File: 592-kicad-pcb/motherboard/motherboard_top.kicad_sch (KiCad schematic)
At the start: 31 parts, among them J21 Conn_02x01, J22 Conn_02x01, J23 Conn_02x01, J24 Conn_02x01, J25 Conn_02x01, J26 Conn_02x01, U15 SN74LVC1G14DBV, U16 SN74LVC1G00DCK, U17 74CBTLV3257PW,118, U18 SN74LVC1G14DBV, U19 74CBTLV3257PW,118, U20 74CBTLV3257PW,118, U21 74CBTLV3257PW,118

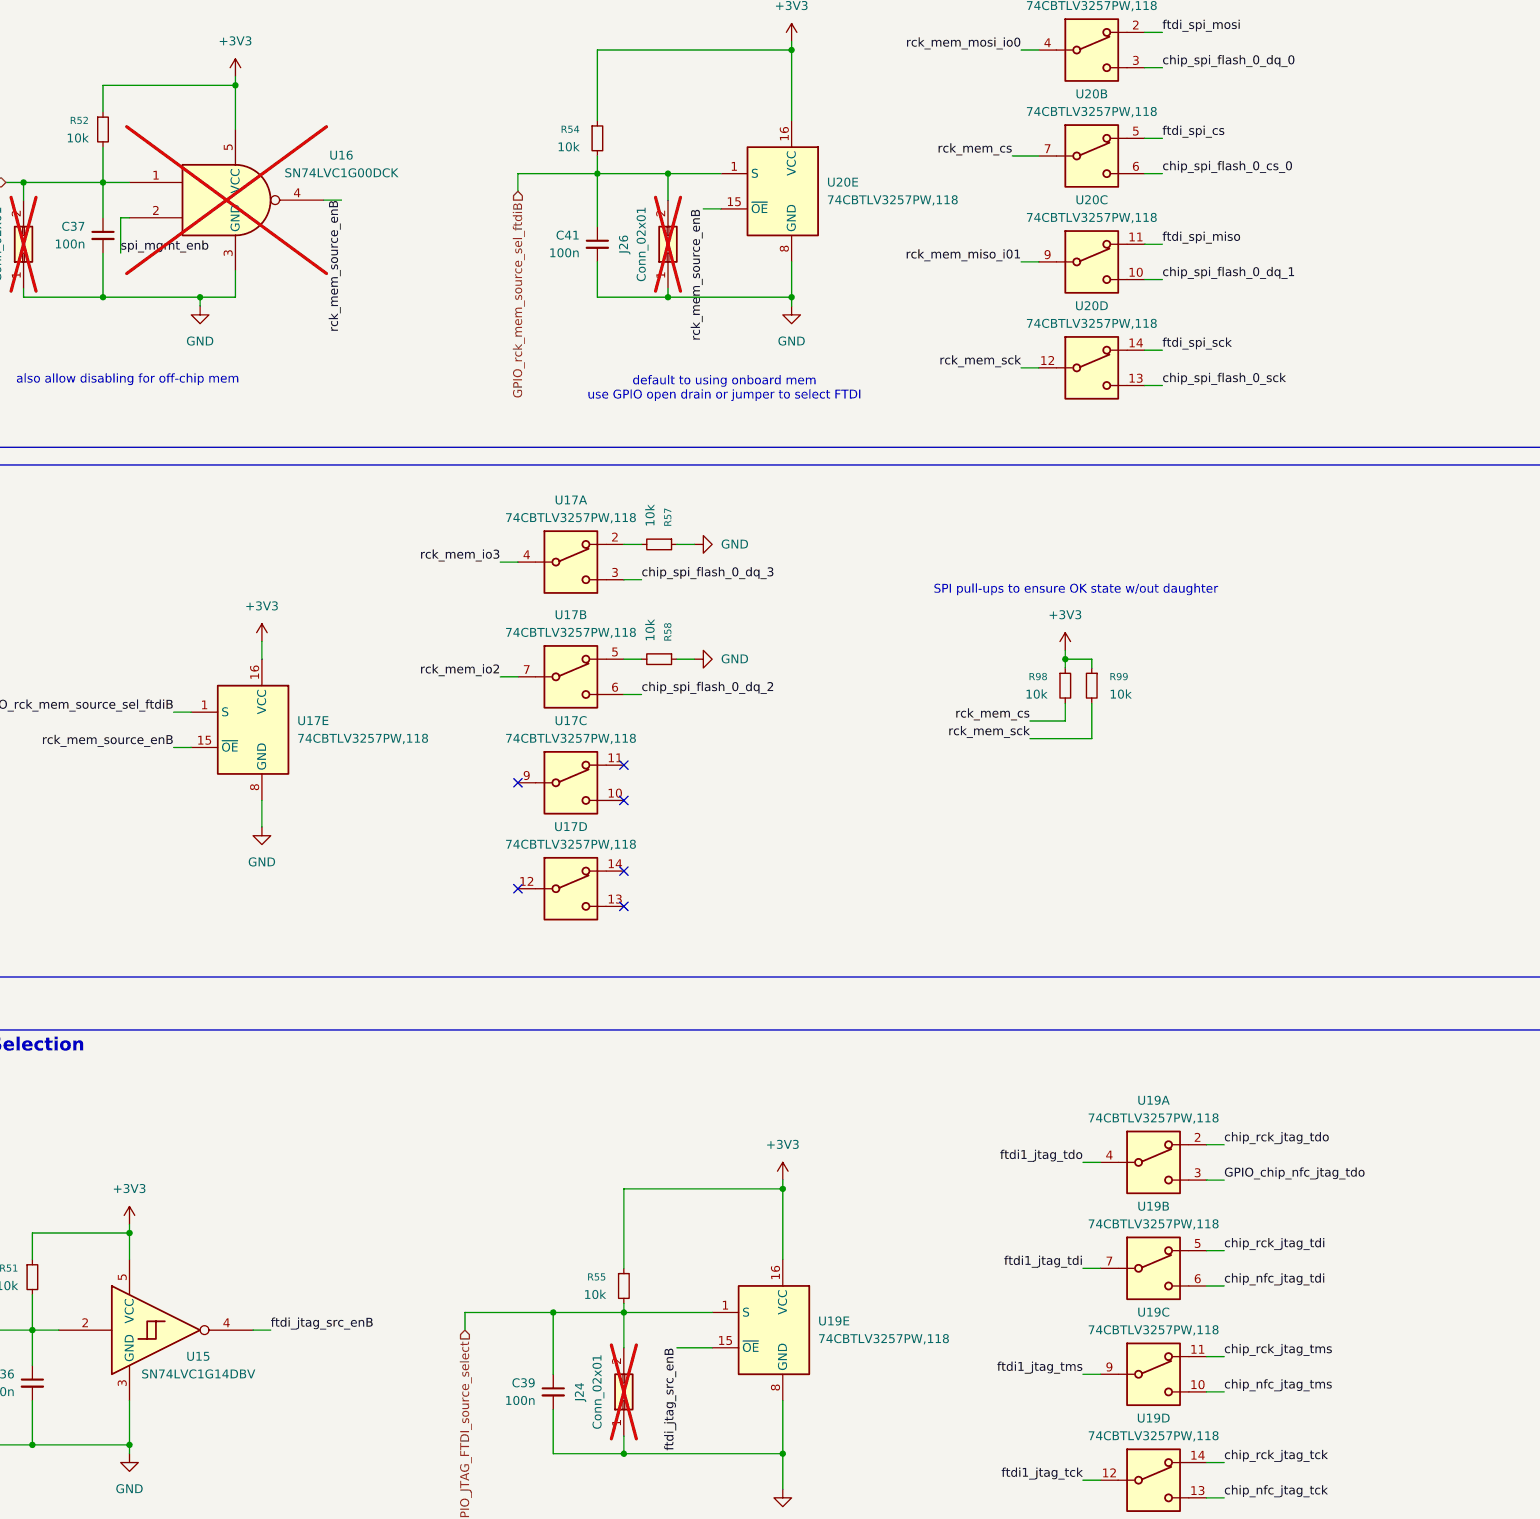
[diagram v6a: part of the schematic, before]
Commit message: core routing progress
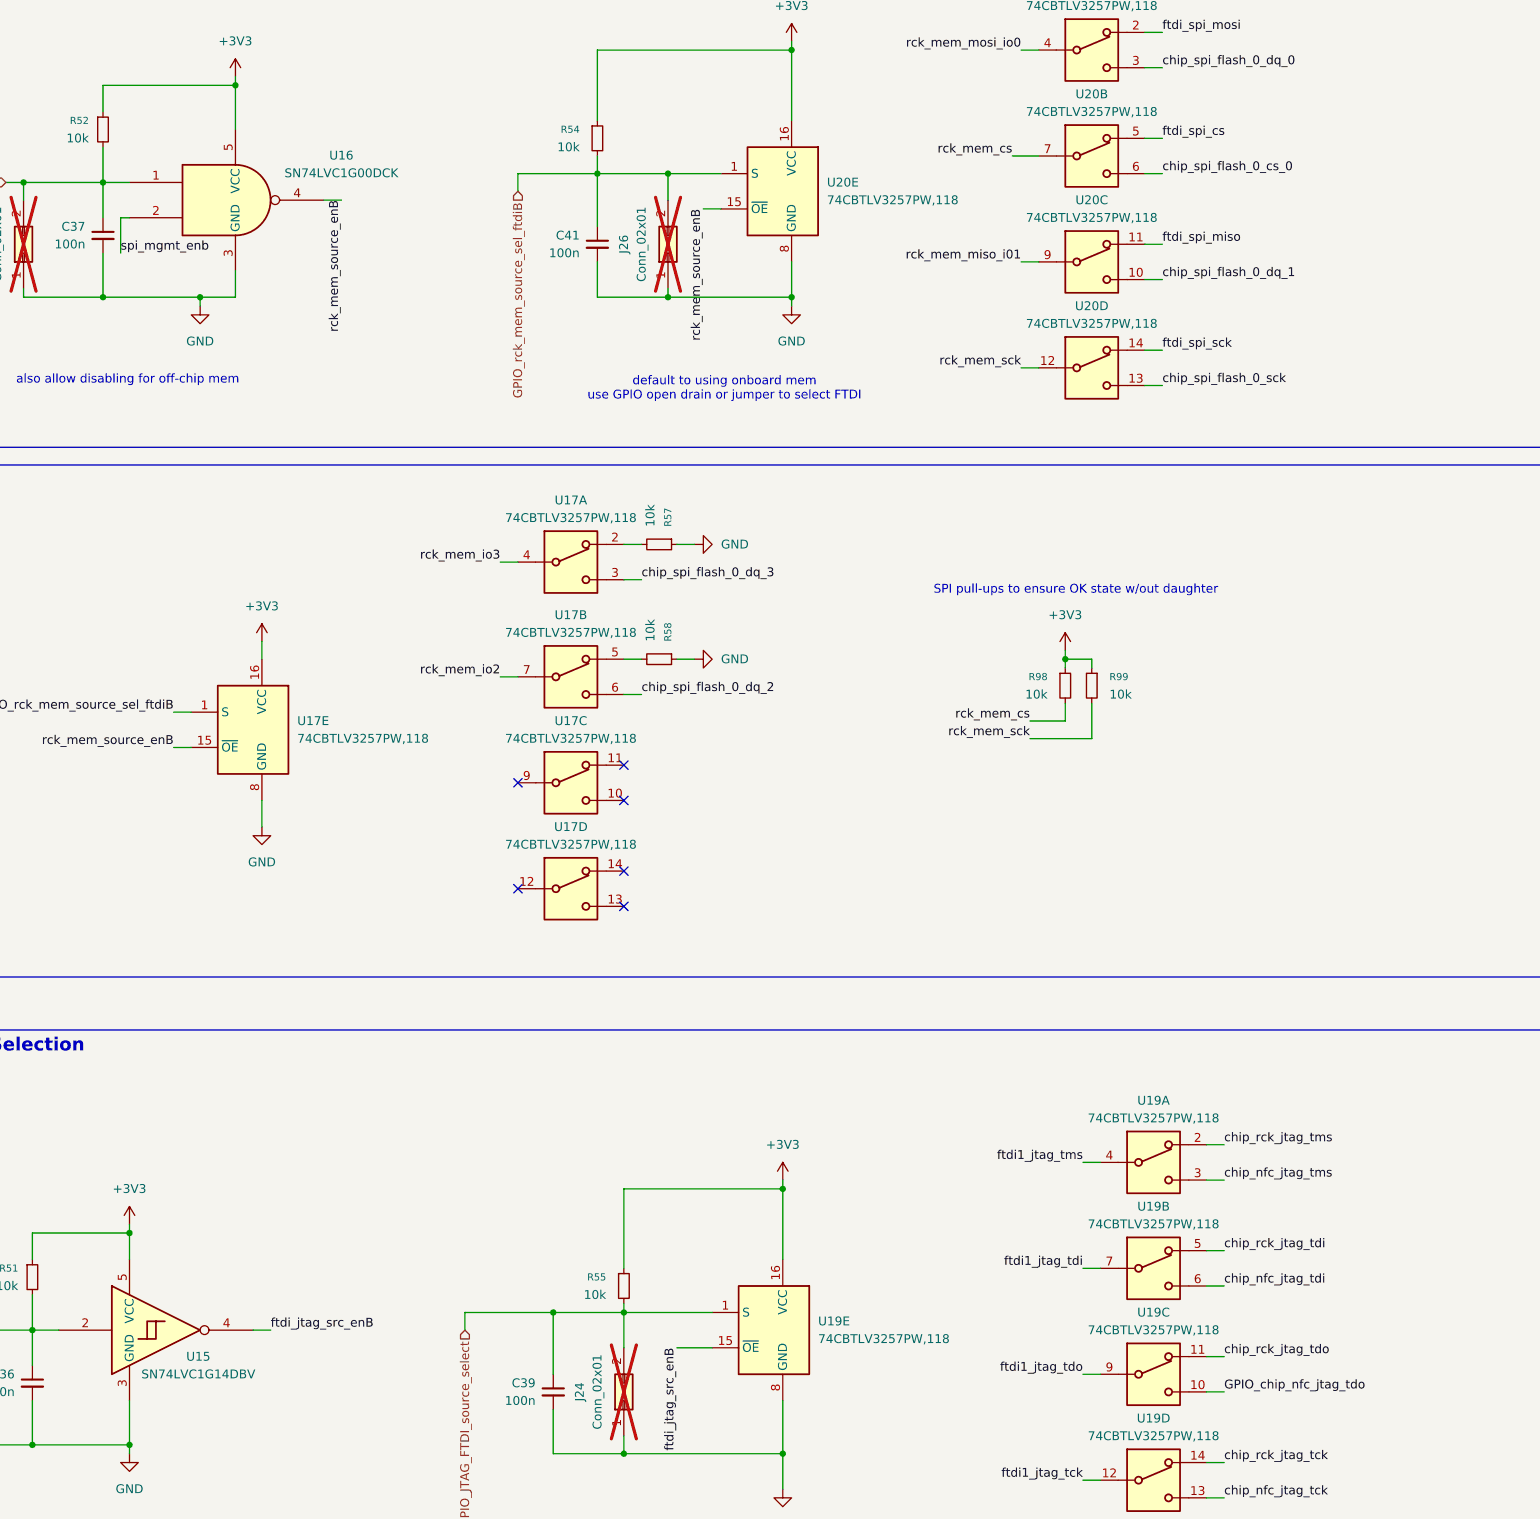
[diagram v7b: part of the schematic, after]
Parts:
- U16: now fitted
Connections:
- net GPIO_chip_nfc_jtag_tdo: now also U19.10; no longer U19.3
- net chip_nfc_jtag_tms: now also U19.3; no longer U19.10
- net chip_rck_jtag_tdo: now also U19.11; no longer U19.2
- net chip_rck_jtag_tms: now also U19.2; no longer U19.11
- net ftdi1_jtag_tdo: now also U19.9; no longer U19.4
- net ftdi1_jtag_tms: now also U19.4; no longer U19.9
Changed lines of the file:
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@@
 	)
 	(label "chip_rck_jtag_tms"
-		(at 491.49 232.41 0)
+		(at 491.49 201.93 0)
 		(effects
 			(font
@@
 	)
 	(label "chip_rck_jtag_tdo"
-		(at 491.49 201.93 0)
+		(at 491.49 232.41 0)
 		(effects
 			(font
@@
 	)
 	(label "GPIO_chip_nfc_jtag_tdo"
-		(at 491.49 207.01 0)
+		(at 491.49 237.49 0)
 		(effects
 			(font
@@
 	)
 	(label "chip_nfc_jtag_tms"
-		(at 491.49 237.49 0)
+		(at 491.49 207.01 0)
 		(effects
 			(font
@@
 	)
 	(label "ftdi1_jtag_tms"
-		(at 471.17 234.95 180)
+		(at 471.17 204.47 180)
 		(effects
 			(font
@@
 	)
 	(label "ftdi1_jtag_tdo"
-		(at 471.17 204.47 180)
+		(at 471.17 234.95 180)
 		(effects
 			(font
@@
 		(in_bom yes)
 		(on_board yes)
-		(dnp yes)
+		(dnp no)
 		(fields_autoplaced yes)
 		(property "Reference" "U16"

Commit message: pins out progress
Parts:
- added J5: Conn_01x04, symbol Connector_Generic:Conn_01x04
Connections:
- new net external_1v8: J5.4 (Pin_4)
- new net external_2v5: J5.3 (Pin_3)
- new net external_3v3: J5.2 (Pin_2)
- new net external_5v: J5.1 (Pin_1)
- no-connect marks 8 -> 7
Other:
- sheet pmic_supplies ports: added 1V8, 1V8_EXT_IN, 2V5, 2V5_EXT_IN, 3V3, 3V3_EXT_IN, 5V0_ON_BOARD, AGND, GND, PG, PGND; removed none
- sheet pmic_switching ports: added 1V8, 2V5, 3V3, 5V0_ON_BOARD, AVAIL, GND, VCCD, VCCD1, VCCD2, VDDA, VDDIO, VDDA1, VDD_EXT, dig_to_adc, gpio_0, gpio_1, gpio_2, gpio_3, ldo_to_adc; removed none
